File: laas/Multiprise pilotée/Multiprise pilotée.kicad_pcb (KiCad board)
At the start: 2 copper layers, 184 x 107.5 mm, 44 parts, among them J1 Conn_01x03, J2 Conn_01x02, J3 Conn_01x02, J4 Conn_01x02, J5 Conn_01x02, J6 Conn_01x03, J7 Conn_02x06_Odd_Even, K1 Omron Relay, K2 Omron Relay, K3 Omron Relay, K4 Omron Relay, Q1 DMN2020LSN-7, Q2 DMN2020LSN-7, Q3 SSM3J355R,LF, Q4 DMN2020LSN-7, Q5 DMN2020LSN-7, Q6 SSM3J355R,LF, Q7 DMN2020LSN-7, Q8 DMN2020LSN-7, U1 MAX4820xUP, U2 74HC595, U4 TC4469, U5 TC4469, U6 TDA7391PD, U7 74AHC1G08, U8 MOUDLE-SEEEDUINO-XIAO

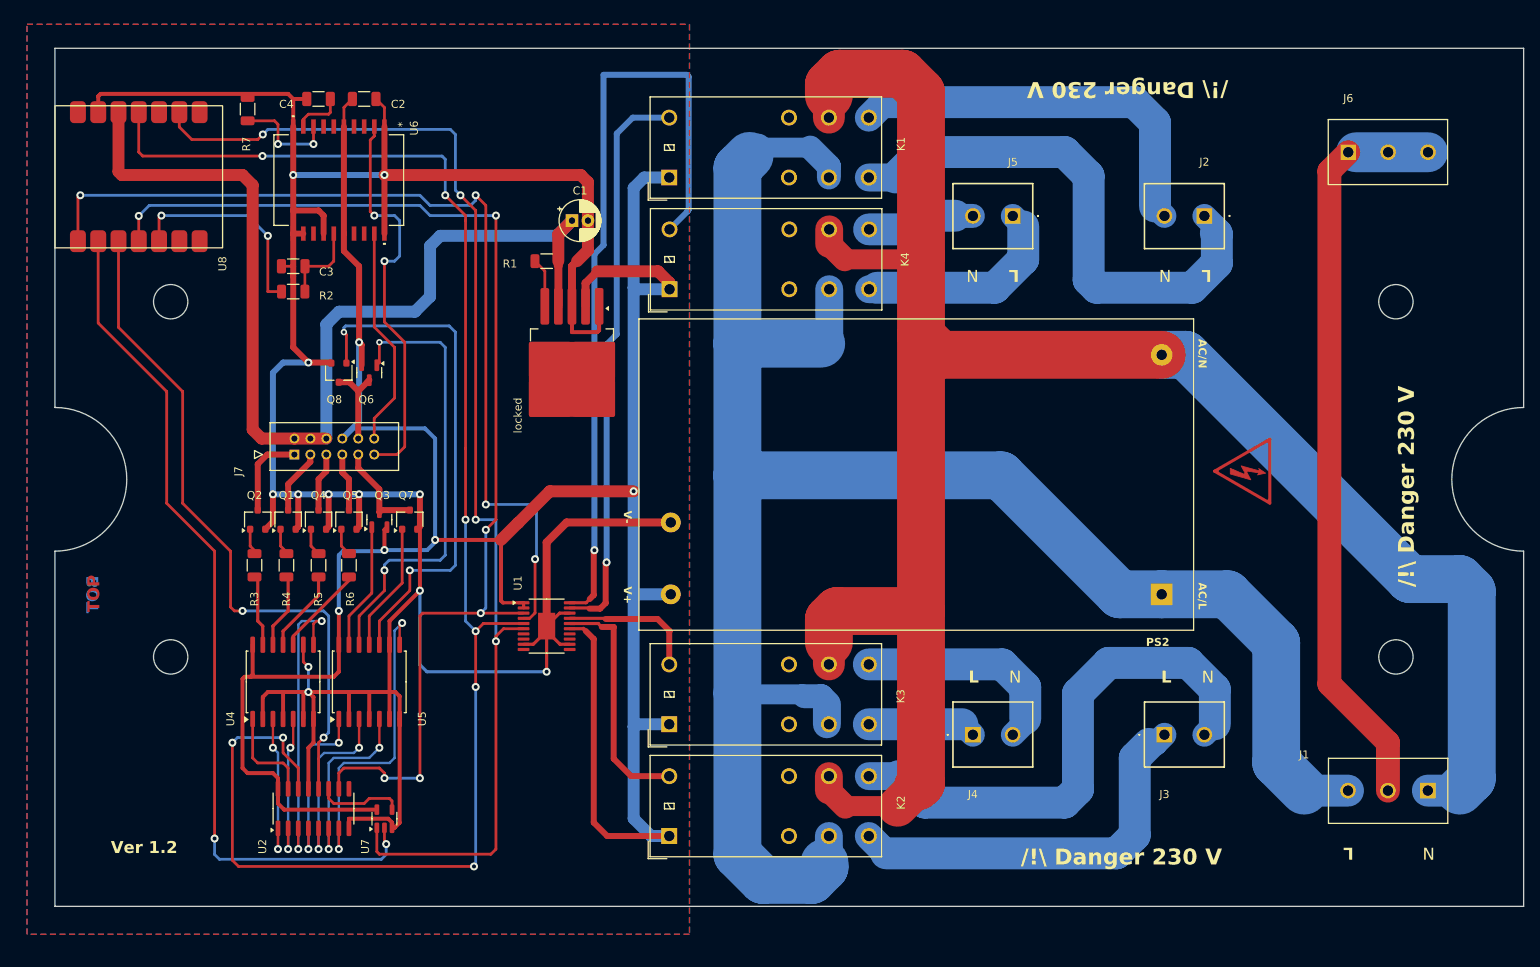
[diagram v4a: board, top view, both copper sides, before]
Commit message: Nouvelle version PCB multiprise 1.3 avec suppresion des alim vpol et var
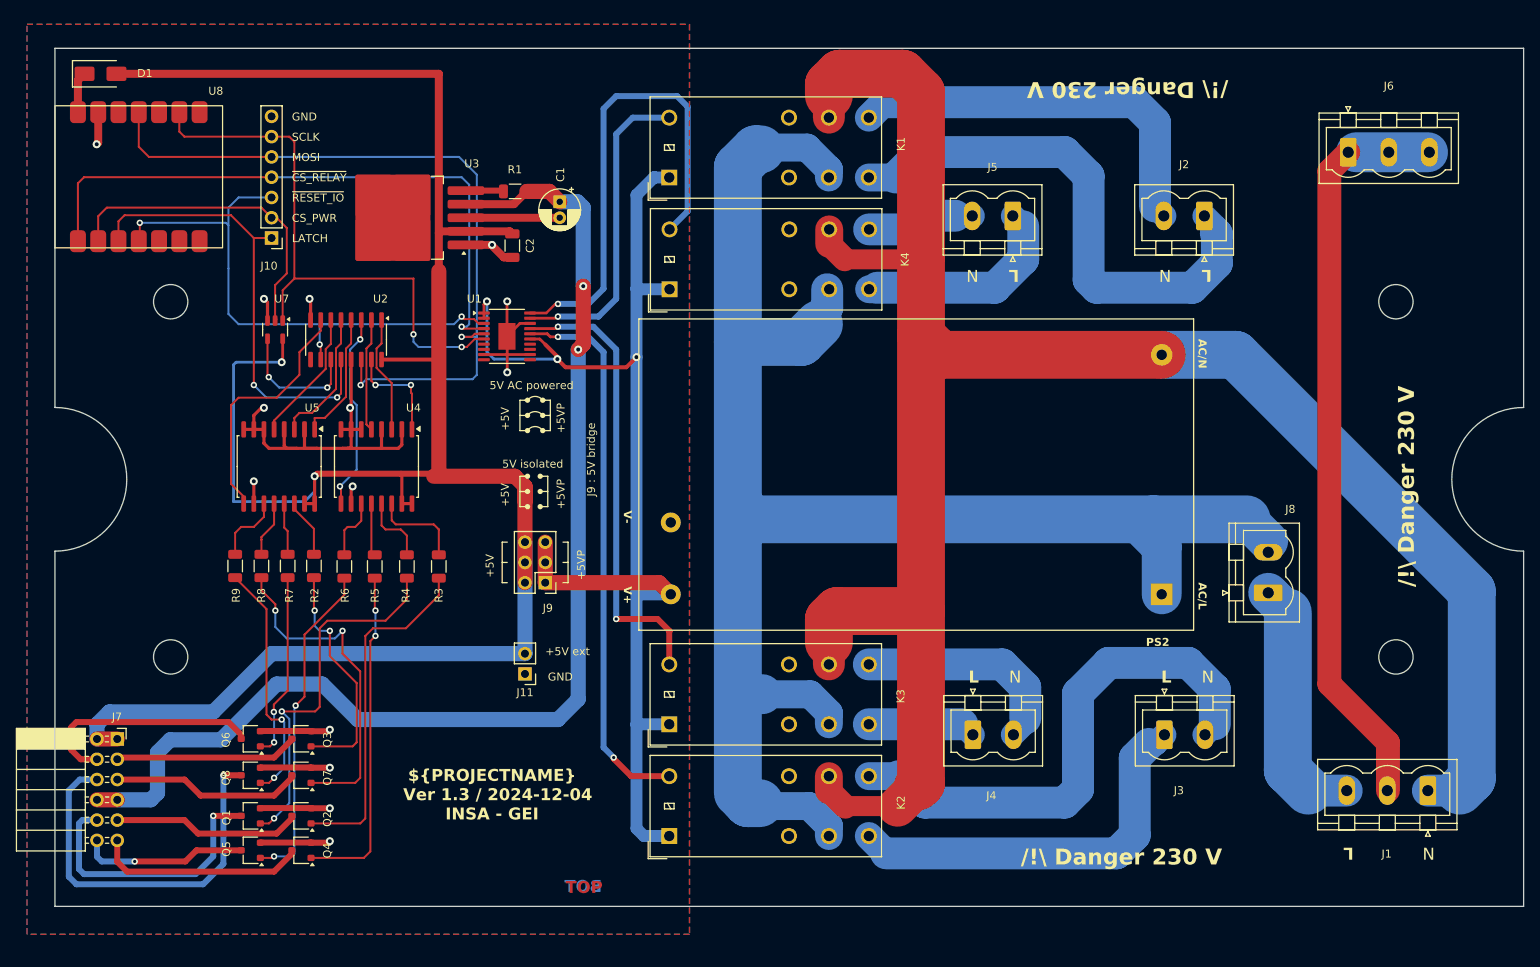
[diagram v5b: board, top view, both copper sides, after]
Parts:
- removed C3: 100nF, Capacitor_SMD:C_1206_3216Metric
- removed C4: 33µF, Capacitor_SMD:C_1206_3216Metric
- removed REF**: Symbol_HighVoltage_Triangle_8x7mm_Copper, Symbol:Symbol_HighVoltage_Triangle_8x7mm_Copper
- removed U6: TDA7391PD, footprints:SO_91PDTR_STM
- added D1: STTH102A, Diode_SMD:D_SMA, F.Cu at (62.7, 44.2)
- added J10: Conn_01x05, Connector_PinHeader_2.54mm:PinHeader_1x07_P2.54mm_Vertical, F.Cu at (84.1, 64.8)
- added J11: Conn_01x02, Connector_PinHeader_2.54mm:PinHeader_1x02_P2.54mm_Vertical, F.Cu at (115.9, 119.4)
- added J8: Conn_01x02, Connector_Phoenix_MSTB:PhoenixContact_MSTBVA_2,5_2-G-5,08_1x02_P5.08mm_Vertical, F.Cu at (209.0, 109.2)
- added J9: Conn_02x03_Odd_Even, Connector_PinHeader_2.54mm:PinHeader_2x03_P2.54mm_Vertical, F.Cu at (118.4, 108.0)
- added R8: 10R, Resistor_SMD:R_1206_3216Metric, F.Cu at (82.9, 105.9)
- added R9: 10R, Resistor_SMD:R_1206_3216Metric, F.Cu at (79.6, 105.9)
- J1, J6: footprint Borniers:5442183 -> Connector_Phoenix_MSTB:PhoenixContact_MSTBVA_2,5_3-G-5,08_1x03_P5.08mm_Vertical
- J2, J3, J4, J5: footprint Borniers:5442170 -> Connector_Phoenix_MSTB:PhoenixContact_MSTBVA_2,5_2-G-5,08_1x02_P5.08mm_Vertical
- J7: footprint Borniers:M80-85312YY -> Connector_PinSocket_2.54mm:PinSocket_2x06_P2.54mm_Horizontal
- Q1, Q2, Q4, Q5, Q7, Q8: value DMN2020LSN-7 -> DMN2020LSN-7
- Q3, Q6: value SSM3J355R,LF -> DMN2020LSN-7; footprint Package_TO_SOT_SMD:SOT-23 -> Package_TO_SOT_SMD:SC-59
- R7: value 56K -> 10R
- U4, U5: footprint Package_SO:SOIC-14W_7.5x9mm_P1.27mm -> Package_SO:SOIC-16W_7.5x10.3mm_P1.27mm
- moved U7 62.8 mm to (84.6, 76.2), turned to -90 degrees
- moved U2 58.9 mm to (93.5, 77.5), turned to -90 degrees
- moved R7 57.5 mm to (86.2, 105.9)
- moved Q8 51.6 mm to (81.5, 132.1), turned to 180 degrees
- moved Q6 48.2 mm to (81.5, 127.5), turned to 180 degrees
- moved Q5 43.2 mm to (81.5, 141.5), turned to 180 degrees
- moved J7 42.0 mm to (64.8, 127.5), turned to 0 degrees
- moved Q4 41.5 mm to (87.9, 141.5), turned to 180 degrees
- moved Q2 37.5 mm to (87.9, 137.2), turned to 180 degrees
- moved Q1 37.4 mm to (81.5, 137.2), turned to 180 degrees
- moved U1 36.6 mm to (113.6, 77.1)
- moved Q7 34.8 mm to (87.9, 132.1), turned to 180 degrees
- moved R2 34.5 mm to (89.4, 105.9), turned to -90 degrees
- moved U4 29.4 mm to (97.3, 93.4), turned to -90 degrees
- moved U5 29.2 mm to (85.1, 93.4), turned to -90 degrees
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- renumbered locked to U3
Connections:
- net /DC supplies/DRV_+5V_A renamed /DC supplies/DRV_5V_1
- net /DC supplies/DRV_+5V_B renamed /DC supplies/DRV_5V_2
- net /DC supplies/DRV_-5V_A renamed /DC supplies/DRV_5V_3
- net Net-(U2-QA) renamed /DC supplies/DRV_3V_1
- net Net-(U2-QB) renamed /DC supplies/DRV_3V_2
- net Net-(U2-QC) renamed /DC supplies/DRV_3V_3
- J1 pad 3: LINE -> Net-(J1-Pin_3)
- J7 pad 1: /DC supplies/PWR_3V3_1 -> +5V
- J7 pad 10: +5V -> /DC supplies/PWR_3V3_2
- J7 pad 11: /DC supplies/PWR_-5V -> /DC supplies/PWR_3V3_3
- J7 pad 12: /DC supplies/PWR_VAR_NEG -> /DC supplies/PWR_3V3_4
- J7 pad 2: /DC supplies/PWR_3V3_2 -> +5V
- J7 pad 3: /DC supplies/PWR_3V3_3 -> /DC supplies/PWR_5V_1
- J7 pad 4: /DC supplies/PWR_5V_1 -> /DC supplies/PWR_5V_2
- J7 pad 5: /DC supplies/PWR_+5V -> /DC supplies/PWR_5V_3
- J7 pad 6: /DC supplies/PWR_VAR_POS -> /DC supplies/PWR_5V_4
- J7 pad 9: +3V3 -> /DC supplies/PWR_3V3_1
- K1 pad A1: +5V -> +5VP
- K2 pad A1: +5V -> +5VP
- K3 pad A1: +5V -> +5VP
- K4 pad A1: +5V -> +5VP
- PS2 pad 4: +5V -> +5VP
- Q3 pad 2: +5V -> GND
- Q3 pad 3: /DC supplies/PWR_+5V -> /DC supplies/PWR_5V_1
- Q5 pad 3: /DC supplies/PWR_5V_1 -> /DC supplies/PWR_3V3_4
- Q6 pad 2: +5V -> GND
- Q6 pad 3: /DC supplies/PWR_-5V -> /DC supplies/PWR_5V_2
- Q7 pad 3: /DC supplies/PWR_+5V -> /DC supplies/PWR_5V_3
- Q8 pad 3: /DC supplies/PWR_-5V -> /DC supplies/PWR_5V_4
- R2 pad 1: /DC supplies/PWM_PWR_VAR -> Net-(U5-1Y)
- R2 pad 2: Net-(U6-IN+) -> Net-(Q3-G)
- R3 pad 1: /DC supplies/DRV_MOS_1 -> Net-(U4-1Y)
- R4 pad 1: /DC supplies/DRV_MOS_2 -> Net-(U4-2Y)
- R5 pad 1: /DC supplies/DRV_MOS_3 -> Net-(U4-3Y)
- R6 pad 1: /DC supplies/DRV_MOS_4 -> Net-(U4-4Y)
- R7 pad 1: GND -> Net-(U5-2Y)
- R7 pad 2: Net-(U6-SYNC) -> Net-(Q6-G)
- U1 pad 1: +5V -> +5VP
- U1 pad 15: +5V -> +5VP
- U1 pad 2: +5V -> +5VP
- U2 pad 3: Net-(U2-QD) -> /DC supplies/DRV_3V_4
- U2 pad 7: /DC supplies/DRV_-5V_B -> /DC supplies/DRV_5V_4
- U4 pad 10: /DC supplies/DRV_MOS_4 -> GND
- U4 pad 11: /DC supplies/DRV_MOS_3 -> Net-(U4-4Y)
- U4 pad 12: /DC supplies/DRV_MOS_2 -> Net-(U4-3Y)
- U4 pad 13: /DC supplies/DRV_MOS_1 -> Net-(U4-2Y)
- U4 pad 14: +5V -> Net-(U4-1Y)
- U4 pad 8: Net-(U2-QD) -> GND
- U4 pad 9: GND -> /DC supplies/DRV_3V_4
- U5 pad 10: Net-(Q8-G) -> GND
- U5 pad 11: Net-(Q7-G) -> Net-(U5-4Y)
- U5 pad 12: Net-(Q6-G) -> Net-(U5-3Y)
- U5 pad 13: Net-(Q3-G) -> Net-(U5-2Y)
- U5 pad 14: +5V -> Net-(U5-1Y)
- U5 pad 8: /DC supplies/DRV_-5V_B -> GND
- U5 pad 9: GND -> /DC supplies/DRV_5V_4
- U8 pad 12: +3V3 -> unconnected-(U8-3V3-Pad12)
- U8 pad 14: unconnected-(U8-5V-Pad14) -> Net-(D1-K)
- U8 pad 5: /DC supplies/PWM_PWR_VAR -> unconnected-(U8-PA8_A4_D4_SDA-Pad5)
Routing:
- net GND: track 389.4 -> 139.2 mm, vias 12 -> 14
- net +5VP: track 0.00 -> 156.3 mm, vias 0 -> 3
- net /DC supplies/MOSI: track 199.6 -> 97.3 mm, vias 8 -> 2
- net /DC supplies/SCLK: track 153.8 -> 72.8 mm, vias 4 -> 2
- net /DC supplies/~{RESET_IO}: track 146.3 -> 73.2 mm, vias 6 -> 3
- net +5V: track 346.2 -> 274.9 mm, vias 5 -> 2
- net /DC supplies/CS_PWR_DC: track 108.4 -> 40.7 mm, vias 2 -> 0
- net /DC supplies/PWR_VAR_POS: track 50.2 -> 0.00 mm, vias 2 -> 0
- net /DC supplies/PWR_5V_4: track 0.00 -> 49.0 mm, vias 0 -> 1
- net Net-(Q1-G): track 3.45 -> 46.5 mm, vias 0 -> 2
- net /DC supplies/DRV_-5V_B: track 40.4 -> 0.00 mm, vias 2 -> 0
- net /Power supply and relays/Relay_3: track 17.4 -> 57.3 mm, vias 0 -> 2
- net Net-(Q2-G): track 3.45 -> 43.4 mm
- net /Power supply and relays/Relay_2: track 30.1 -> 69.5 mm, vias 0 -> 2
- net /MCU/~{CS_RELAY}: track 117.4 -> 78.4 mm, vias 4 -> 1
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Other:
- board text added: "${PROJECTNAME} Ver ${REVISION} / ${ISSUE_DATE} ${COMPANY}"
- board text added: "+5V"
- board text added: "+5V ext"
- board text added: "+5VP"
- board text added: "5V AC powered"
- board text added: "5V isolated"
- board text added: "CS_PWR"
- board text added: "GND"
- board text added: "J9 : 5V bridge"
- board text added: "LATCH"
- board text added: "MOSI"
- board text added: "SCLK"
- board text added: "~{CS_RELAY}"
- board text added: "~{RESET_IO}"
- board text removed: "Ver 1.2"
